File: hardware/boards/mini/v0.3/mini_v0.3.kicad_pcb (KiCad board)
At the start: 8 copper layers, 20 x 40 mm, 95 parts, among them IC1 NAU88C22YG, IC3 IS42S16160J-6BLI, J1 Connector, U1 W25Q128JVP, U2 LTV-217-G, U4 STM32H750XBHx, Y1 Crystal_GND24, Y3 32.768kHz

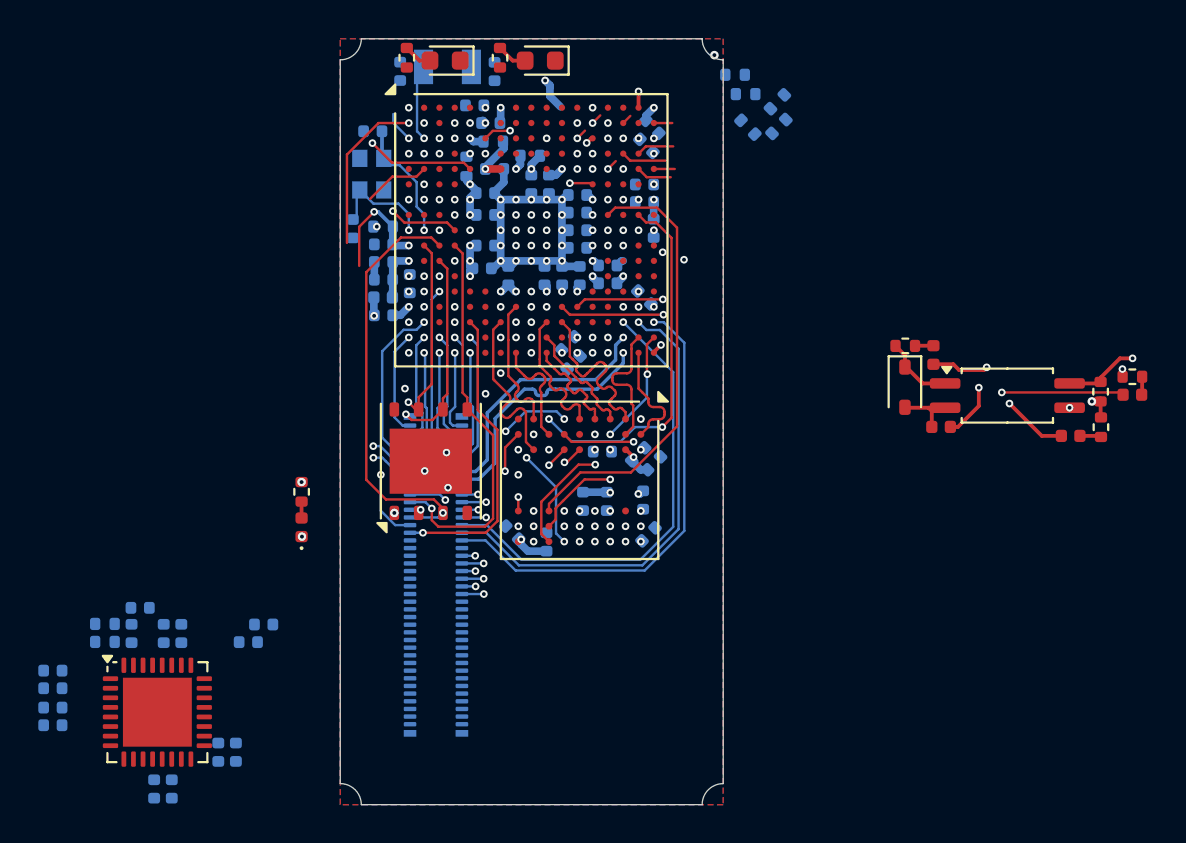
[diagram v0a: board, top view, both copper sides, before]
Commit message: mini: SWD, SPI, and audio codec layout
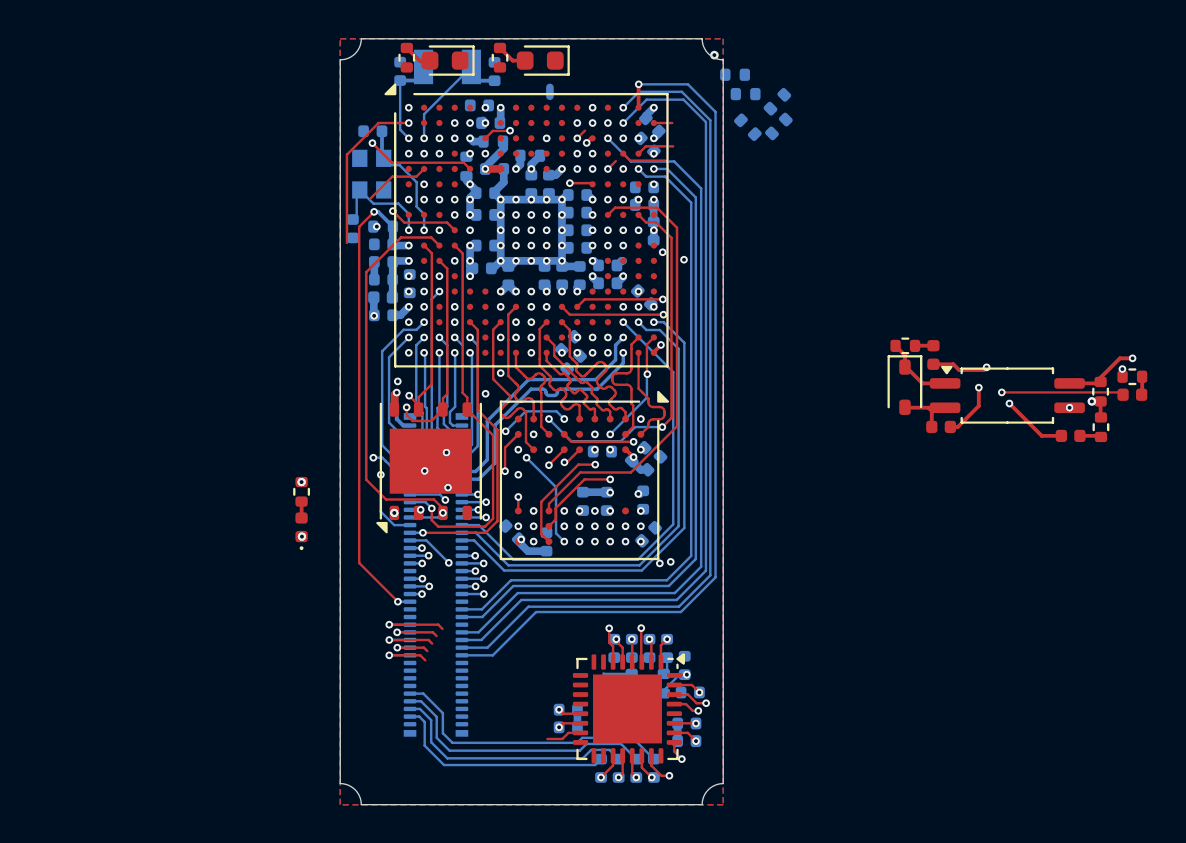
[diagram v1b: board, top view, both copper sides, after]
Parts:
- moved C22 32.1 mm to (87.1, 88.8), turned to 90 degrees
- moved C23 31.2 mm to (86.2, 88.8), turned to 90 degrees
- moved C24 30.4 mm to (85.2, 88.8), turned to 90 degrees
- moved C25 29.6 mm to (84.3, 88.8), turned to 90 degrees
- moved R4 29.4 mm to (86.9, 90.7), turned to -90 degrees
- moved C19 29.3 mm to (88.3, 91.1), turned to 180 degrees
- moved C28 28.6 mm to (88.0, 89.7), turned to 90 degrees
- moved C29 27.7 mm to (88.1, 92.8), turned to 180 degrees
- moved R3 27.6 mm to (85.2, 90.7), turned to -90 degrees
- moved C18 27.0 mm to (88.1, 93.7), turned to 180 degrees
- moved IC1 24.6 mm to (85.0, 92.0), turned to -90 degrees
- moved C20 22.2 mm to (86.4, 95.1), turned to 90 degrees
- moved C17 22.0 mm to (81.9, 92.0), turned to 0 degrees
- moved C16 21.0 mm to (81.9, 93.0), turned to 0 degrees
- moved C21 20.9 mm to (85.5, 95.1), turned to 90 degrees
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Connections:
- C20 pad 2: /AUX_OUT_L -> /AUX_OUT_R
- C21 pad 2: /AUX_OUT_R -> /AUX_OUT_L
- J1 pad 1: unconnected-(J1-Pin_1-Pad1) -> +3.3V
- J1 pad 10: unconnected-(J1-Pin_10-Pad10) -> /PB1
- J1 pad 11: unconnected-(J1-Pin_11-Pad11) -> /PC3
- J1 pad 12: unconnected-(J1-Pin_12-Pad12) -> GND
- J1 pad 14: unconnected-(J1-Pin_14-Pad14) -> /USB_D+
- J1 pad 16: unconnected-(J1-Pin_16-Pad16) -> /USB_D-
- J1 pad 18: unconnected-(J1-Pin_18-Pad18) -> GND
- J1 pad 19: unconnected-(J1-Pin_19-Pad19) -> /QSPI_CLK
- J1 pad 2: unconnected-(J1-Pin_2-Pad2) -> /PC5
- J1 pad 20: unconnected-(J1-Pin_20-Pad20) -> /PH7
- J1 pad 21: unconnected-(J1-Pin_21-Pad21) -> /QSPI_IO0
- J1 pad 22: unconnected-(J1-Pin_22-Pad22) -> /PH8
- J1 pad 23: unconnected-(J1-Pin_23-Pad23) -> /QSPI_IO1
- J1 pad 24: unconnected-(J1-Pin_24-Pad24) -> /PB13
- J1 pad 25: unconnected-(J1-Pin_25-Pad25) -> /QSPI_IO2
- J1 pad 26: unconnected-(J1-Pin_26-Pad26) -> /PB12
- J1 pad 27: unconnected-(J1-Pin_27-Pad27) -> /QSPI_IO3
- J1 pad 28: unconnected-(J1-Pin_28-Pad28) -> /PD11
- J1 pad 29: unconnected-(J1-Pin_29-Pad29) -> /EXT_QSPI_DETECT
- J1 pad 3: unconnected-(J1-Pin_3-Pad3) -> /PA0
- J1 pad 30: unconnected-(J1-Pin_30-Pad30) -> /PD12
- J1 pad 31: unconnected-(J1-Pin_31-Pad31) -> /QSPI_CS_EXP
- J1 pad 32: unconnected-(J1-Pin_32-Pad32) -> /PD13
- J1 pad 33: GND -> /PK1
- J1 pad 34: unconnected-(J1-Pin_34-Pad34) -> GND
- J1 pad 35: /SDMMC1_D2 -> /PK0
- J1 pad 36: unconnected-(J1-Pin_36-Pad36) -> /SDMMC1_D0
- J1 pad 37: /SDMMC1_D3 -> /PJ11
- J1 pad 38: unconnected-(J1-Pin_38-Pad38) -> /SDMMC1_D1
- J1 pad 39: /SDMMC1_CK -> GND
- J1 pad 4: unconnected-(J1-Pin_4-Pad4) -> /PA5
- J1 pad 40: unconnected-(J1-Pin_40-Pad40) -> /SDMMC1_CMD
- J1 pad 41: /SDMMC1_CMD -> /SWD_IO
- J1 pad 42: unconnected-(J1-Pin_42-Pad42) -> /SDMMC1_CK
- J1 pad 43: /SDMMC1_D1 -> /SWD_CLK
- J1 pad 44: unconnected-(J1-Pin_44-Pad44) -> /SDMMC1_D3
- J1 pad 45: /SDMMC1_D0 -> /SWD_SWO
- J1 pad 46: unconnected-(J1-Pin_46-Pad46) -> /SDMMC1_D2
- J1 pad 47: GND -> /RST
- J1 pad 48: unconnected-(J1-Pin_48-Pad48) -> GND
- J1 pad 49: /PD13 -> /BOOT0
- J1 pad 5: unconnected-(J1-Pin_5-Pad5) -> /PA1
- J1 pad 50: /QSPI_CS_EXP -> /PA12/4TX
- J1 pad 51: /PD12 -> GND
- J1 pad 52: /EXT_QSPI_DETECT -> /PA11/4RX
- J1 pad 53: /PD11 -> /SAI1_SD_B
- J1 pad 54: /QSPI_IO3 -> GND
- J1 pad 55: /PB12 -> /SAI1_SCK
- J1 pad 56: /QSPI_IO2 -> /SPI_MOSI
- J1 pad 57: /PB13 -> /SAI1_FS
- J1 pad 58: /QSPI_IO1 -> /SPI_MISO
- J1 pad 59: /PH8 -> /SAI1_MCLK
- J1 pad 6: unconnected-(J1-Pin_6-Pad6) -> /PA4
- J1 pad 60: /QSPI_IO0 -> /SPI_SCK
- J1 pad 61: /PH7 -> /SAI1_SD_A
- J1 pad 62: /QSPI_CLK -> /SPI_NSS
- J1 pad 63: GND -> unconnected-(J1-Pin_63-Pad63)
- J1 pad 64: unconnected-(J1-Pin_64-Pad64) -> GND
- J1 pad 65: /USB_D- -> unconnected-(J1-Pin_65-Pad65)
- J1 pad 67: /USB_D+ -> unconnected-(J1-Pin_67-Pad67)
- J1 pad 69: GND -> unconnected-(J1-Pin_69-Pad69)
- J1 pad 7: unconnected-(J1-Pin_7-Pad7) -> /PA3
- J1 pad 71: /PB1 -> /AUX_OUT_R
- J1 pad 72: /PC3 -> unconnected-(J1-Pin_72-Pad72)
- J1 pad 73: /PB0 -> /AUX_OUT_L
- J1 pad 74: /PA2 -> unconnected-(J1-Pin_74-Pad74)
- J1 pad 75: /PA4 -> /AUX_IN_R
- J1 pad 76: /PA3 -> unconnected-(J1-Pin_76-Pad76)
- J1 pad 77: /PA5 -> /AUX_IN_L
- J1 pad 78: /PA1 -> unconnected-(J1-Pin_78-Pad78)
- J1 pad 79: /PC5 -> GND
- J1 pad 8: unconnected-(J1-Pin_8-Pad8) -> /PB0
- J1 pad 80: /PA0 -> +3.3V
- J1 pad 9: unconnected-(J1-Pin_9-Pad9) -> /PA2
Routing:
- net /SWD_SWO: track 4.86 -> 52.4 mm, vias 1 -> 2
- net /SPI_NSS: track 0.85 -> 45.1 mm
- net /SWD_CLK: track 0.00 -> 43.9 mm, vias 1 -> 2
- net /SPI_SCK: track 0.00 -> 43.8 mm, vias 0 -> 1
- net /SPI_MISO: track 0.52 -> 43.0 mm, vias 0 -> 1
- net /SWD_IO: track 0.28 -> 41.9 mm, vias 1 -> 2
- net /SPI_MOSI: track 0.00 -> 39.6 mm
- net /PA11/4RX: track 1.09 -> 35.2 mm, vias 0 -> 1
- net /PA12/4TX: track 1.86 -> 35.1 mm, vias 0 -> 1
- net /RST: track 6.23 -> 25.2 mm, vias 2 -> 3
- net /AUX_OUT_R: track 0.00 -> 15.0 mm
- net /AUX_OUT_L: track 0.00 -> 14.0 mm
- net /AUX_IN_R: track 0.00 -> 13.0 mm
- net /AUX_IN_L: track 0.00 -> 11.9 mm
- net /QSPI_CS_EXP: track 27.9 -> 37.1 mm, vias 1 -> 2
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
